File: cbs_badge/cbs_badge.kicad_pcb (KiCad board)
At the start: 2 copper layers, 38.1 x 38.1 mm, 13 parts, among them J1 AVR-ISP-6, SW1 TOUCH, U1 ATtiny45-20SU

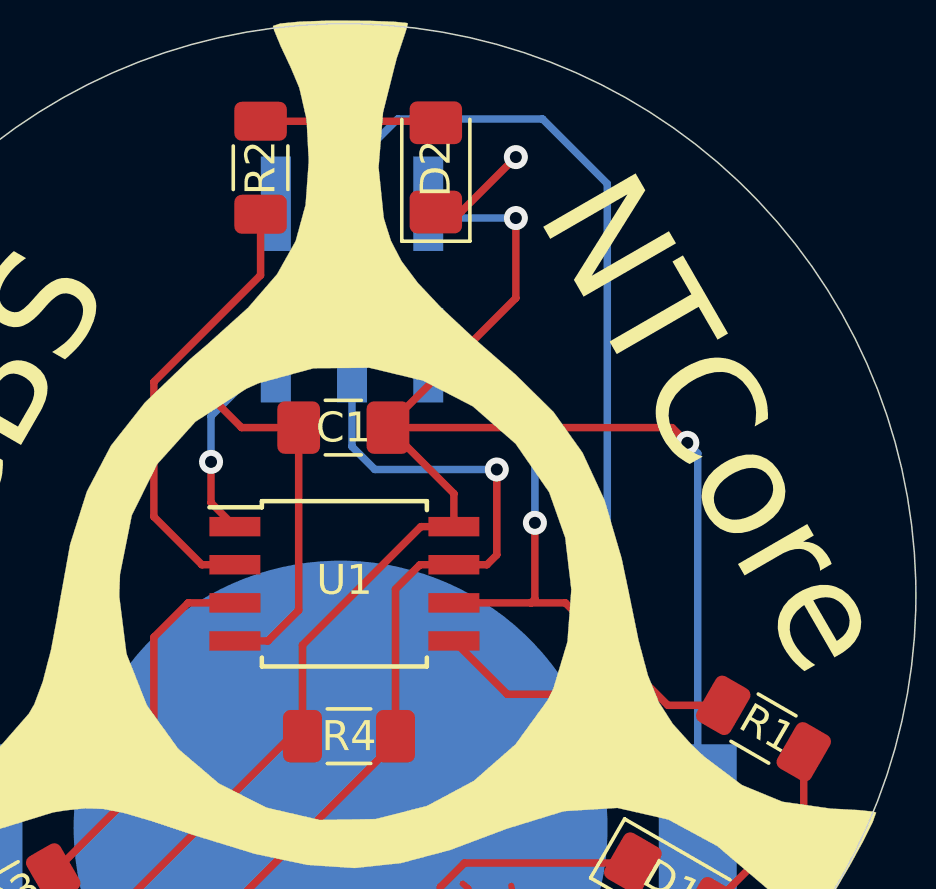
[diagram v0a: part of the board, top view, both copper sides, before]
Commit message: minor routing changes
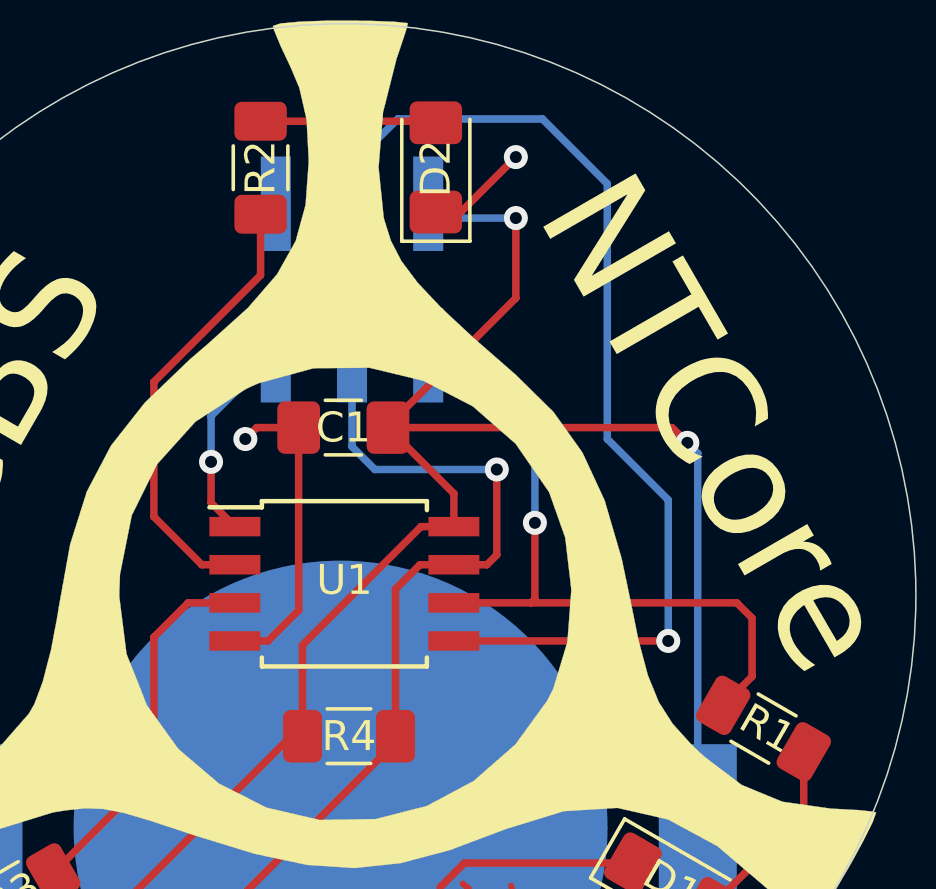
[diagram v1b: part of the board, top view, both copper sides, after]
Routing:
- net /PB1_MISO_LED1: track 20.7 -> 23.8 mm
- net GND: track 35.1 -> 32.8 mm
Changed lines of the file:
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@@
     (thickness 1.6)
     (drawings 75)
-    (tracks 93)
+    (tracks 95)
     (zones 0)
     (modules 13)
@@
     (35 F.Paste user hide)
     (36 B.SilkS user)
-    (37 F.SilkS user hide)
+    (37 F.SilkS user)
     (38 B.Mask user hide)
     (39 F.Mask user hide)
@@
   (segment (start 187.271 101.019) (end 189.103 99.187) (width 0.25) (layer F.Cu) (net 1))
   (segment (start 186.436 101.019) (end 187.271 101.019) (width 0.25) (layer F.Cu) (net 1))
-  (via (at 178.308 106.553) (size 0.8) (drill 0.4) (layers F.Cu B.Cu) (net 1))
-  (segment (start 179.959 108.204) (end 178.308 106.553) (width 0.25) (layer F.Cu) (net 1))
-  (segment (start 181.864 108.204) (end 179.959 108.204) (width 0.25) (layer F.Cu) (net 1))
   (via (at 170.434 115.062) (size 0.8) (drill 0.4) (layers F.Cu B.Cu) (net 1))
   (segment (start 170.434 117.856) (end 170.434 115.062) (width 0.25) (layer F.Cu) (net 1))
@@
   (segment (start 180.838 115.316) (end 181.864 114.29) (width 0.25) (layer F.Cu) (net 1))
   (segment (start 179.738 115.316) (end 180.838 115.316) (width 0.25) (layer F.Cu) (net 1))
+  (via (at 180.086 108.585) (size 0.8) (drill 0.4) (layers F.Cu B.Cu) (net 1))
+  (segment (start 180.467 108.204) (end 180.086 108.585) (width 0.25) (layer F.Cu) (net 1))
+  (segment (start 181.864 108.204) (end 180.467 108.204) (width 0.25) (layer F.Cu) (net 1))
   (segment (start 187.038 110.403) (end 184.839 108.204) (width 0.25) (layer F.Cu) (net 2))
   (segment (start 187.038 111.506) (end 187.038 110.403) (width 0.25) (layer F.Cu) (net 2))
@@
   (segment (start 185.166 97.917) (end 189.992 97.917) (width 0.25) (layer B.Cu) (net 6))
   (segment (start 189.992 97.917) (end 192.151 100.076) (width 0.25) (layer B.Cu) (net 6))
-  (via (at 192.151 117.094) (size 0.8) (drill 0.4) (layers F.Cu B.Cu) (net 6))
-  (segment (start 192.151 100.076) (end 192.151 117.094) (width 0.25) (layer B.Cu) (net 6))
-  (segment (start 188.816 117.094) (end 187.038 115.316) (width 0.25) (layer F.Cu) (net 6))
-  (segment (start 192.151 117.094) (end 188.816 117.094) (width 0.25) (layer F.Cu) (net 6))
+  (via (at 194.183 115.316) (size 0.8) (drill 0.4) (layers F.Cu B.Cu) (net 6))
+  (segment (start 187.038 115.316) (end 194.183 115.316) (width 0.25) (layer F.Cu) (net 6))
+  (segment (start 194.183 115.316) (end 194.183 110.617) (width 0.25) (layer B.Cu) (net 6))
+  (segment (start 192.151 108.585) (end 192.151 100.076) (width 0.25) (layer B.Cu) (net 6))
+  (segment (start 194.183 110.617) (end 192.151 108.585) (width 0.25) (layer B.Cu) (net 6))
   (segment (start 181.102 105.791) (end 180.975 105.791) (width 0.25) (layer B.Cu) (net 7))
   (via (at 178.943 109.347) (size 0.8) (drill 0.4) (layers F.Cu B.Cu) (net 7))
@@
   (segment (start 178.943 110.711) (end 179.738 111.506) (width 0.25) (layer F.Cu) (net 7))
   (segment (start 178.943 109.347) (end 178.943 110.711) (width 0.25) (layer F.Cu) (net 7))
-  (segment (start 196.015661 117.462) (end 194.17 117.462) (width 0.25) (layer F.Cu) (net 8))
-  (segment (start 194.17 117.462) (end 190.754 114.046) (width 0.25) (layer F.Cu) (net 8))
   (segment (start 186.182 105.791) (end 187.071 105.791) (width 0.25) (layer B.Cu) (net 8))
   (via (at 189.738 111.379) (size 0.8) (drill 0.4) (layers F.Cu B.Cu) (net 8))
@@
   (segment (start 189.738 111.379) (end 189.738 113.919) (width 0.25) (layer F.Cu) (net 8))
   (segment (start 189.611 114.046) (end 187.038 114.046) (width 0.25) (layer F.Cu) (net 8))
-  (segment (start 190.754 114.046) (end 189.611 114.046) (width 0.25) (layer F.Cu) (net 8))
+  (segment (start 196.977 116.500661) (end 196.015661 117.462) (width 0.25) (layer F.Cu) (net 8))
+  (segment (start 196.977 114.554) (end 196.977 116.500661) (width 0.25) (layer F.Cu) (net 8))
+  (segment (start 196.469 114.046) (end 196.977 114.554) (width 0.25) (layer F.Cu) (net 8))
+  (segment (start 189.611 114.046) (end 196.469 114.046) (width 0.25) (layer F.Cu) (net 8))
   (segment (start 185.091 118.491) (end 185.091 113.59) (width 0.25) (layer F.Cu) (net 9))
   (segment (start 185.905 112.776) (end 187.038 112.776) (width 0.25) (layer F.Cu) (net 9))

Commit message: ordered from oshpark
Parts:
- moved U1 0.38 mm to (183.4, 113.8)
- moved D3 0.22 mm to (169.2, 118.4)
- moved BT1 0.13 mm to (183.4, 121.5)
- moved J1 0.13 mm to (183.5, 103.3)
- moved R2 0.13 mm to (180.5, 99.5)
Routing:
- net GND: track 32.8 -> 23.2 mm, vias 4 -> 5
- net /PB4_LED3: track 12.4 -> 11.9 mm
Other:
- rule pad_to_mask_clearance: 0 -> 0.000051
- rule trace_min: 0.2 -> 0.1524
- rule via_min_drill: 0.3 -> 0.254
- rule via_min_size: 0.4 -> 0.508
